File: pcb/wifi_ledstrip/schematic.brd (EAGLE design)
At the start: 80 x 49.5 mm, 65 parts, among them IC1 STM32F10XCXT6, Q1 8MHz

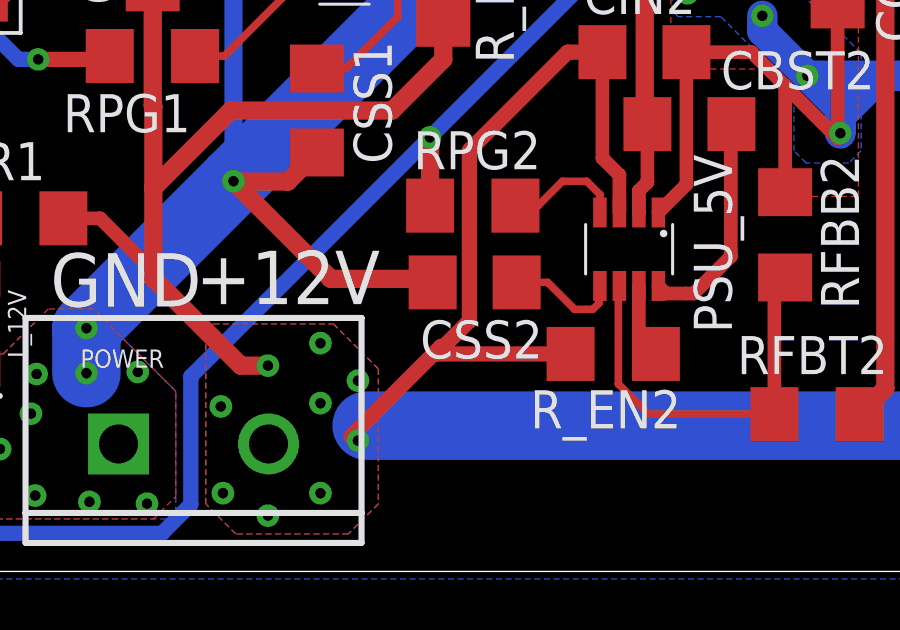
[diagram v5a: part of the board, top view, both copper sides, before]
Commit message: capacitor moved a bit
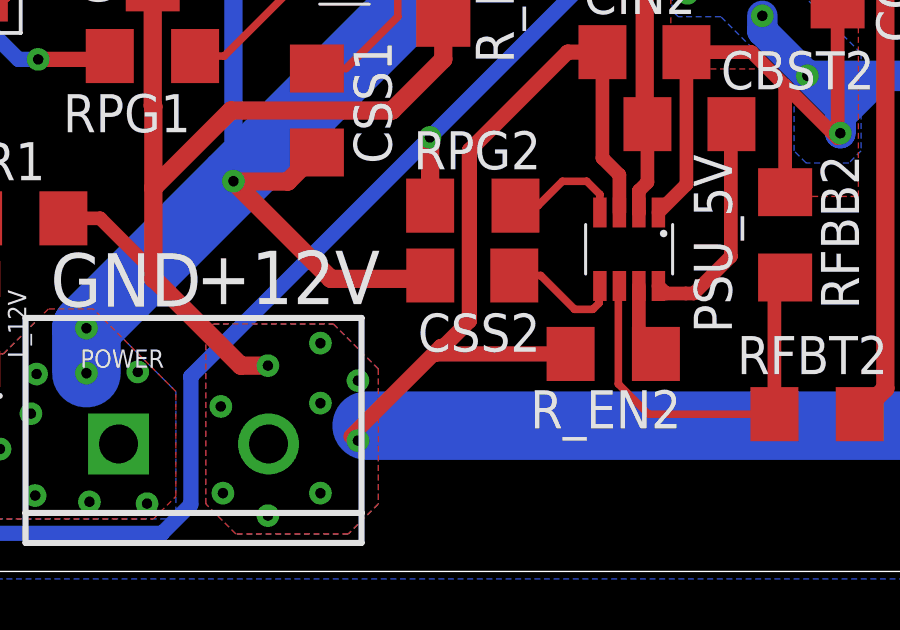
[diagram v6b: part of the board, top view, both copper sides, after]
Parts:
- moved CSS2 0.24 mm to (24.6, 9.87)
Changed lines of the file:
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@@
 <attribute name="VALUE" x="29.1" y="14.77" size="1.27" layer="27"/>
 </element>
-<element name="CSS2" library="rcl" library_urn="urn:adsk.eagle:library:334" package="C1206" package3d_urn="urn:adsk.eagle:package:23618/2" value="100n" x="24.7108" y="9.6356" smashed="yes" rot="R180">
-<attribute name="NAME" x="26.9808" y="8.3656" size="1.27" layer="25" rot="R180"/>
-<attribute name="SPICEPREFIX" value="C" x="37.4108" y="13.4456" size="1.778" layer="27" rot="R180" display="off"/>
-<attribute name="VALUE" x="25.9808" y="12.1756" size="1.27" layer="27" rot="R180"/>
+<element name="CSS2" library="rcl" library_urn="urn:adsk.eagle:library:334" package="C1206" package3d_urn="urn:adsk.eagle:package:23618/2" value="100n" x="24.6308" y="9.8656" smashed="yes" rot="R180">
+<attribute name="NAME" x="26.9008" y="8.5956" size="1.27" layer="25" rot="R180"/>
+<attribute name="SPICEPREFIX" value="C" x="37.3308" y="13.6756" size="1.778" layer="27" rot="R180" display="off"/>
+<attribute name="VALUE" x="25.9008" y="12.4056" size="1.27" layer="27" rot="R180"/>
 </element>
 <element name="CBST2" library="rcl" library_urn="urn:adsk.eagle:library:334" package="C1206" package3d_urn="urn:adsk.eagle:package:23618/2" value="100n" x="31.87" y="14.91" smashed="yes">
@@
 <contactref element="CSS1" pad="2"/>
 <contactref element="CSS2" pad="2"/>
-<wire x1="23.1928" y1="9.7536" x2="23.3108" y2="9.6356" width="0.6096" layer="1"/>
-<wire x1="23.1928" y1="9.7536" x2="19.9136" y2="9.7536" width="0.6096" layer="1"/>
+<wire x1="23.1188" y1="9.7536" x2="23.2308" y2="9.8656" width="0.6096" layer="1"/>
+<wire x1="23.1188" y1="9.7536" x2="19.9136" y2="9.7536" width="0.6096" layer="1"/>
 <wire x1="16.67" y1="12.9972" x2="16.67" y2="13.01" width="0.6096" layer="1"/>
 <wire x1="19.9136" y1="9.7536" x2="16.67" y2="12.9972" width="0.6096" layer="1"/>
@@
 <wire x1="28.8544" y1="8.9408" x2="28.6512" y2="8.7376" width="0.254" layer="1"/>
 <wire x1="28.6512" y1="8.7376" x2="28.0416" y2="8.7376" width="0.254" layer="1"/>
-<wire x1="28.0416" y1="8.7376" x2="27.1436" y2="9.6356" width="0.254" layer="1"/>
-<wire x1="27.1436" y1="9.6356" x2="26.1108" y2="9.6356" width="0.254" layer="1"/>
+<wire x1="28.0416" y1="8.7376" x2="26.9136" y2="9.8656" width="0.254" layer="1"/>
+<wire x1="26.9136" y1="9.8656" x2="26.0308" y2="9.8656" width="0.254" layer="1"/>
 </signal>
 <signal name="N$31">
